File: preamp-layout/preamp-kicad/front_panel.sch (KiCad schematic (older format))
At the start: 42 parts, among them J54 Conn_01x04_Male, J55 Conn_01x04_Male, J74 Conn_01x03_Female, J75 Conn_01x03_Female, J76 Conn_01x03_Female, J77 Conn_01x03_Female, J78 Conn_01x03_Female, J79 Conn_01x03_Female, J80 Conn_01x03_Female, J81 Conn_01x03_Female, J84 Conn_01x05_Female, SW11 Rotary_Encoder_Switch, SW12 Rotary_Encoder_Switch, U23 MCP23017_SO

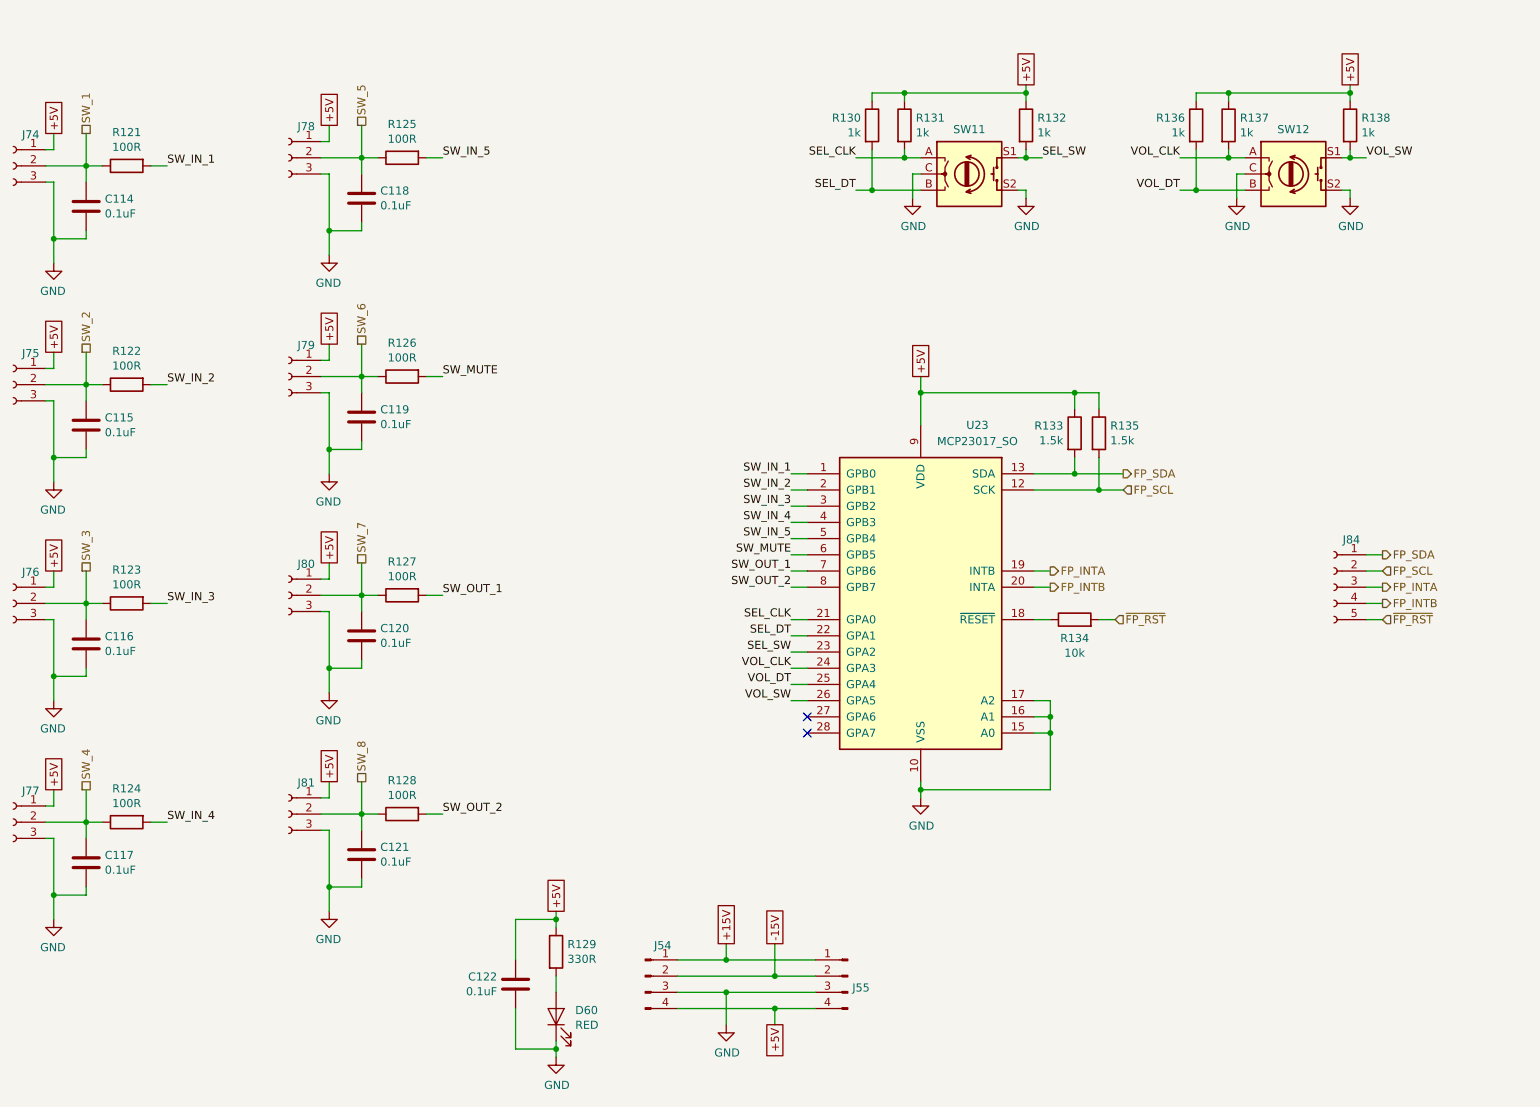
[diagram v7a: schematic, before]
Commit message: PCB layout update, front panel and LED restructure
Restructure of capacitive buttons. Restructure of MCU schematic. Moved LEDs to front panel sheet. Front panel and MCU initial PCB layout. 8 bit DAC update (grounded address pins). DAC connection renaming. Added mounting holes for boards.
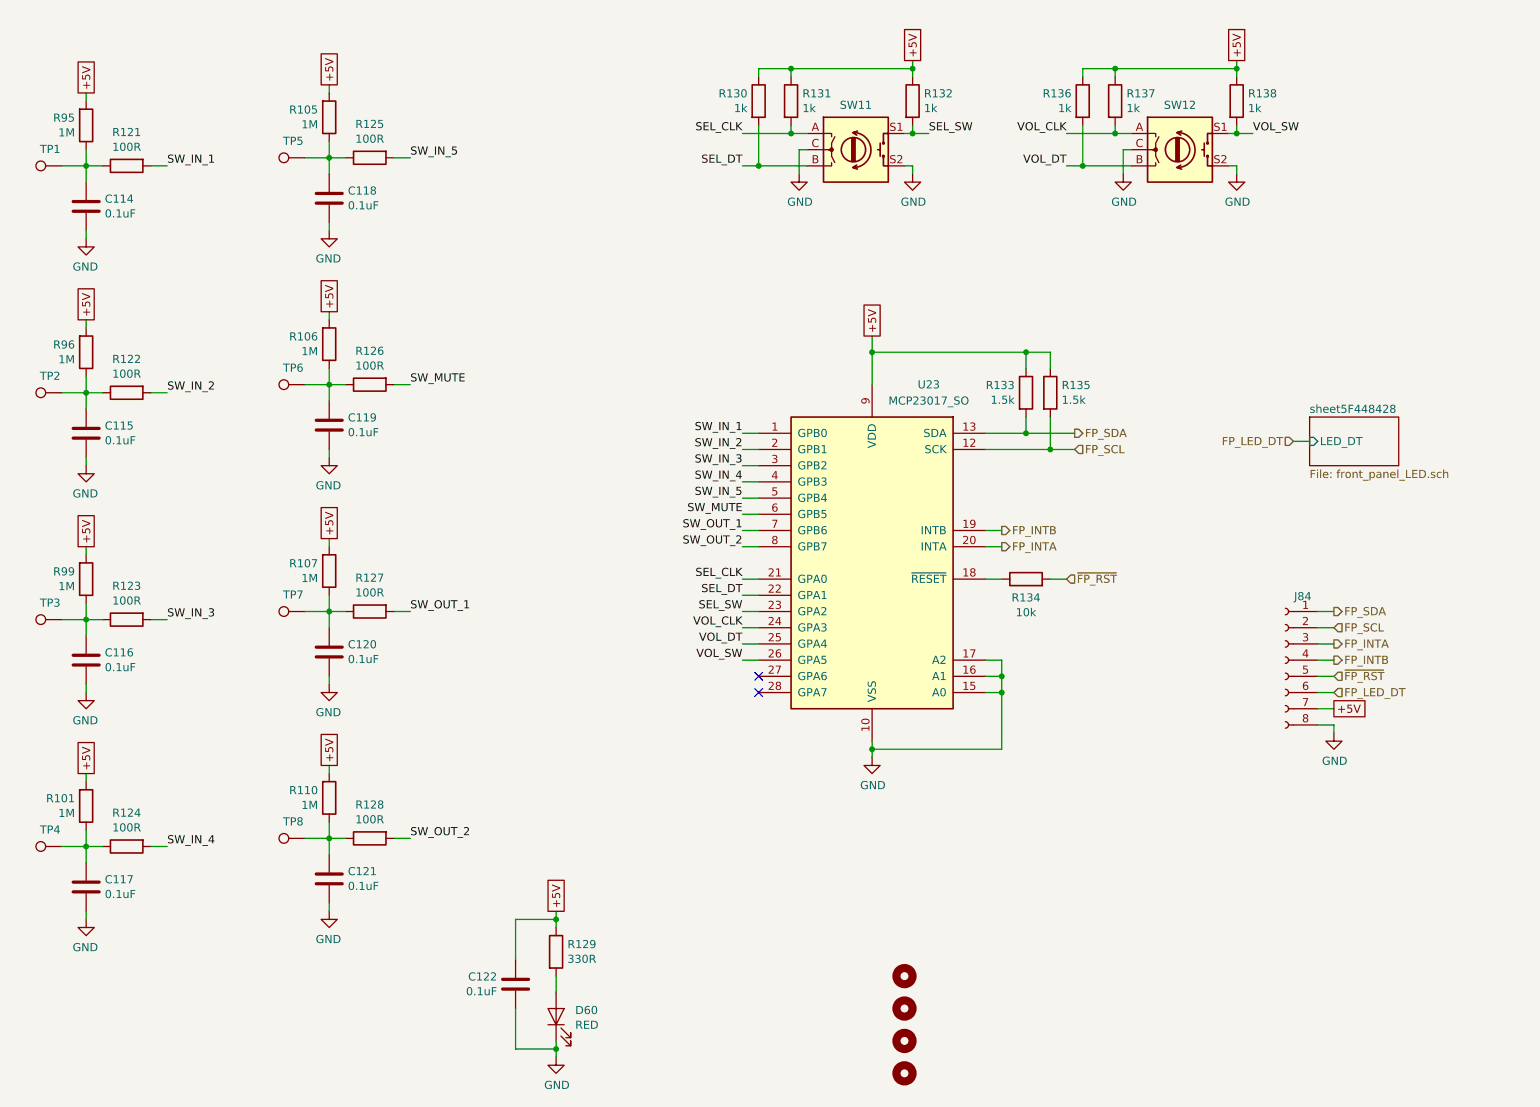
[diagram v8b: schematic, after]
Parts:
- removed J54, J55: Conn_01x04_Male, Connector_JST:JST_EH_S4B-EH_1x04_P2.50mm_Horizontal, symbol Connector:Conn_01x04_Male
- removed J74, J75, J76, J77, J78, J79, J80, J81: Conn_01x03_Female, Connector_PinHeader_2.54mm:PinHeader_1x03_P2.54mm_Vertical, symbol Connector:Conn_01x03_Female
- removed J84: Conn_01x05_Female, Connector_PinHeader_2.54mm:PinHeader_1x05_P2.54mm_Vertical, symbol Connector:Conn_01x05_Female
- added H33, H34, H35, H36: MountingHole, MountingHole:MountingHole_3.2mm_M3, symbol Mechanical:MountingHole
- added J84: Conn_01x08_Female, Connector_JST:JST_EH_B8B-EH-A_1x08_P2.50mm_Vertical, symbol Connector:Conn_01x08_Female
- added R101, R105, R106, R107, R110, R95, R96, R99: 1M, Resistor_SMD:R_1206_3216Metric_Pad1.42x1.75mm_HandSolder, symbol Device:R
- added TP1, TP2, TP3, TP4, TP5, TP6, TP7, TP8: TestPoint, symbol Connector:TestPoint
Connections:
- net +5V: now also J84.7 (Pin_7), R101.2, R105.2, R106.2, R107.2, R110.2, R95.2, R96.2, R99.2
- net FP_INTA: now also U23.20 (INTA), J84.3 (Pin_3); no longer U23.19 (INTB)
- net FP_INTB: now also U23.19 (INTB), J84.4 (Pin_4); no longer U23.20 (INTA)
- net FP_SCL: now also J84.2 (Pin_2)
- net FP_SDA: now also J84.1 (Pin_1)
- net GND: now also J84.8 (Pin_8)
- net ~FP_RST: now also J84.5 (Pin_5)
- net SW_1: no longer names the net of C114.1, R121.1
- net SW_1: now also R95.1, TP1.1
- net SW_2: no longer names the net of C115.1, R122.1
- net SW_2: now also R96.1, TP2.1
- net SW_3: no longer names the net of C116.1, R123.1
- net SW_3: now also R99.1, TP3.1
- net SW_4: no longer names the net of C117.1, R124.1
- net SW_4: now also R101.1, TP4.1
- net SW_5: no longer names the net of C118.1, R125.1
- net SW_5: now also R105.1, TP5.1
- net SW_6: no longer names the net of C119.1, R126.1
- net SW_6: now also R106.1, TP6.1
- net SW_7: no longer names the net of C120.1, R127.1
- net SW_7: now also R107.1, TP7.1
- net SW_8: no longer names the net of C121.1, R128.1
- net SW_8: now also R110.1, TP8.1
- new net FP_LED_DT: J84.6 (Pin_6)
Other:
- moved on the sheet: C115, C116, C117, C118, C119, C120, C121, R122, R123, R124, R125, R126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
